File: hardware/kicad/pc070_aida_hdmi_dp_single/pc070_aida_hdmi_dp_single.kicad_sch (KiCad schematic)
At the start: 2 parts

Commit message: Minor tidying of artwork
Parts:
- J1: value (none) -> 47272-0001; footprint (none) -> 47272-0001:MOLEX_47272-0001
- J2: value (none) -> HDMR-19-01-S-SM-TR; footprint (none) -> HDMR-19-01-S-SM-TR:SAMTEC_HDMR-19-01-S-SM-TR
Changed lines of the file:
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@@
     (in_bom yes) (on_board yes) (fields_autoplaced)
     (property "Reference" "J1" (id 0) (at 139.7 54.7202 0))
-    (property "Value" "" (id 1) (at 139.7 57.2571 0))
-    (property "Footprint" "" (id 2) (at 139.7 86.36 0)
+    (property "Value" "47272-0001" (id 1) (at 139.7 57.2571 0))
+    (property "Footprint" "47272-0001:MOLEX_47272-0001" (id 2) (at 139.7 86.36 0)
       (effects (font (size 1.27 1.27)) (justify left bottom) hide)
     )
@@
       (effects (font (size 1.27 1.27)) (justify left))
     )
-    (property "Value" "" (id 1) (at 181.61 57.15 0)
+    (property "Value" "HDMR-19-01-S-SM-TR" (id 1) (at 181.61 57.15 0)
       (effects (font (size 1.27 1.27)) (justify left))
     )
-    (property "Footprint" "" (id 2) (at 189.23 86.36 0)
+    (property "Footprint" "HDMR-19-01-S-SM-TR:SAMTEC_HDMR-19-01-S-SM-TR" (id 2) (at 189.23 86.36 0)
       (effects (font (size 1.27 1.27)) (justify left bottom) hide)
     )

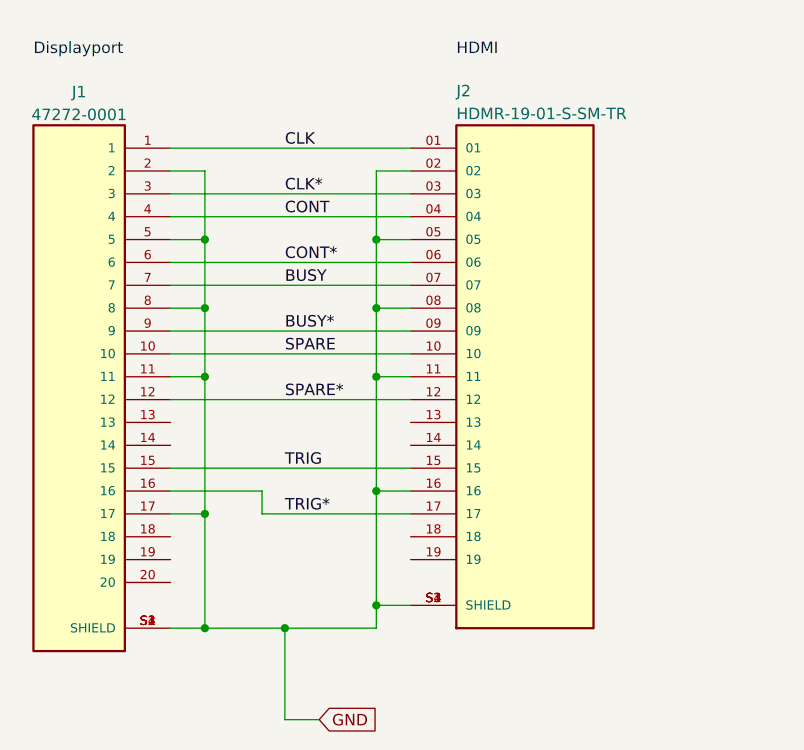
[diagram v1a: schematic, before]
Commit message: Producing artwork for bug-fixed bodge board
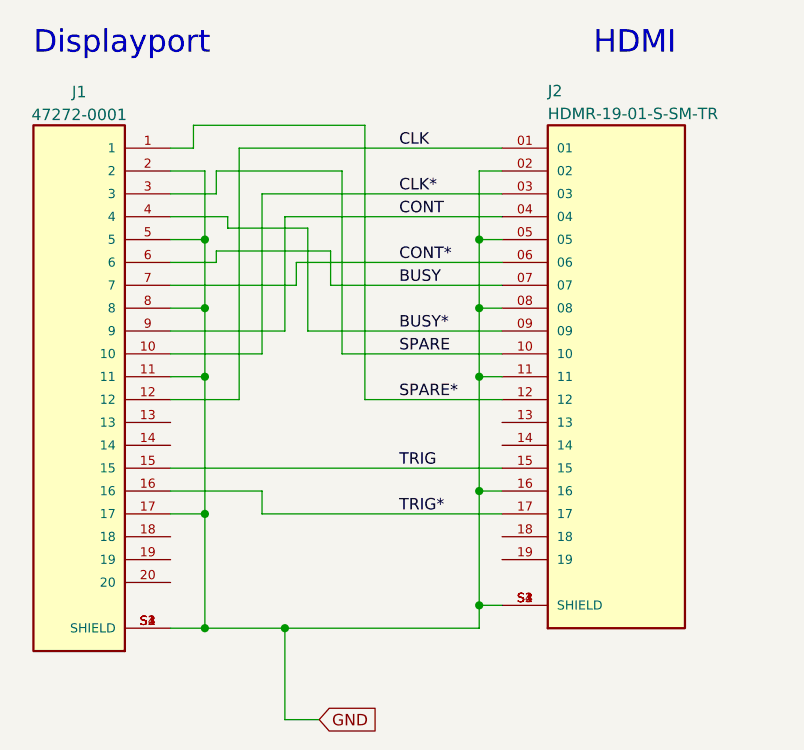
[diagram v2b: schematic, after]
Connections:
- net BUSY: now also J1.6; no longer J1.7
- net BUSY*: now also J1.4; no longer J1.9
- net CLK: now also J1.12; no longer J1.1
- net CLK*: now also J1.10; no longer J1.3
- net CONT: now also J1.9; no longer J1.4
- net CONT*: now also J1.7; no longer J1.6
- net SPARE: now also J1.3; no longer J1.10
- net SPARE*: now also J1.1; no longer J1.12
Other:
- moved on the sheet: J2

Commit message: Committing artwork for v3 of the adaptor board
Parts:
- added TP1, TP10, TP11, TP12, TP2, TP3, TP4, TP5, TP6, TP7, TP8, TP9: TestPoint, TestPoint:TestPoint_THTPad_1.0x1.0mm_Drill0.5mm, symbol Connector:TestPoint
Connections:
- net BUSY: now also TP7.1
- net BUSY*: now also TP8.1
- net CLK: now also TP3.1
- net CLK*: now also TP4.1
- net CONT: now also TP9.1
- net CONT*: now also TP10.1
- net GND: now also J1.16, TP1.1, TP2.1; no longer J1.17, J2.16
- net SPARE: now also TP11.1
- net SPARE*: now also TP12.1
- net TRIG: now also TP5.1
- net TRIG*: now also J1.17, J2.16, TP6.1; no longer J1.16, J2.17
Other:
- note added: "Pinout for AIDA-2020 TLU on HDMI"
- note added: "Pinout for AIDA-Innova TLU (remember Display port cable is cross-over for lanes 0-3)"
